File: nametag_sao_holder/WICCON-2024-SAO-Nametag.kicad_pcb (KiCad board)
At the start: 2 copper layers, 150 x 137.2 mm, 20 parts, among them J1 Conn_02x03_Odd_Even, J2 Conn_02x03_Odd_Even, J3 Conn_02x03_Odd_Even, J4 Conn_02x03_Odd_Even, J5 Conn_02x03_Odd_Even, J6 Conn_02x03_Odd_Even, J7 Conn_02x03_Odd_Even, J8 Conn_02x03_Odd_Even, SW1 ON/OFF, U1 QX2303L33E

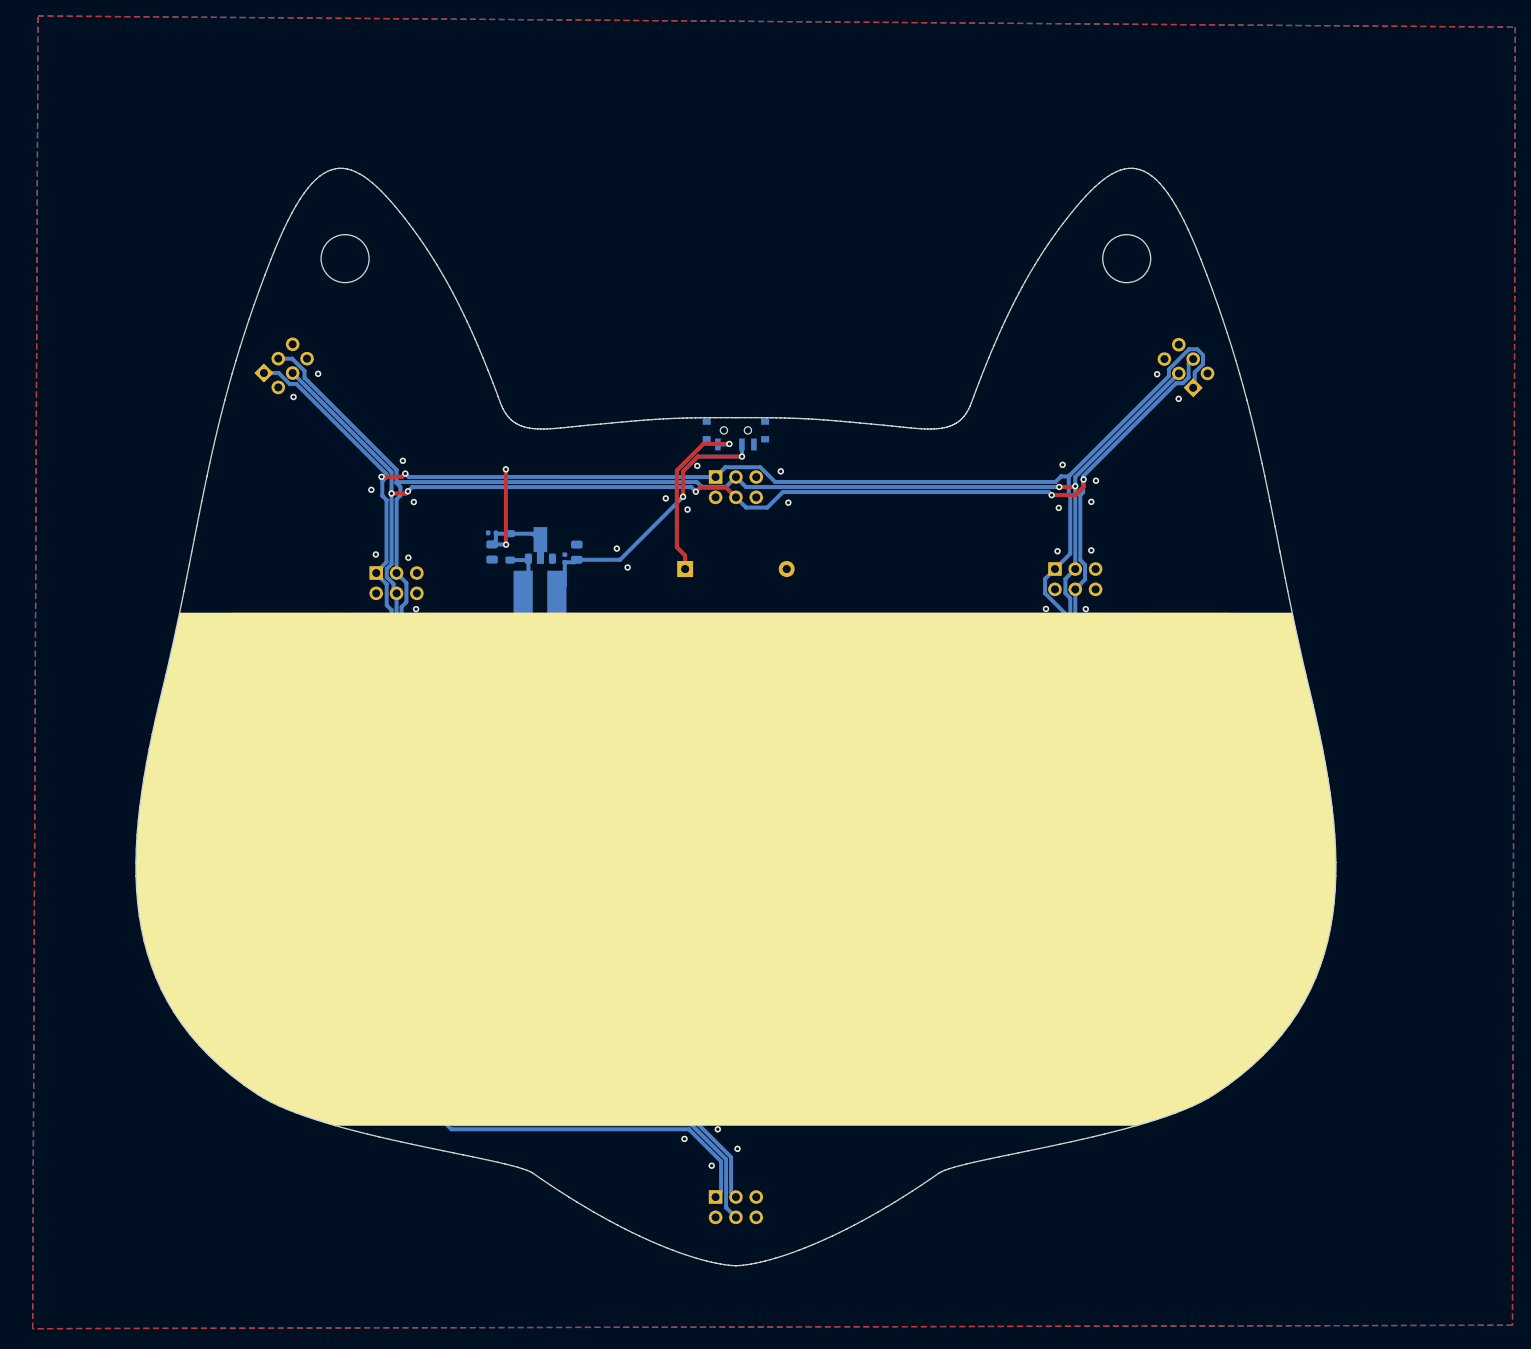
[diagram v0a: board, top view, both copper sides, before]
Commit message: Apply some improvements based on review by Paul
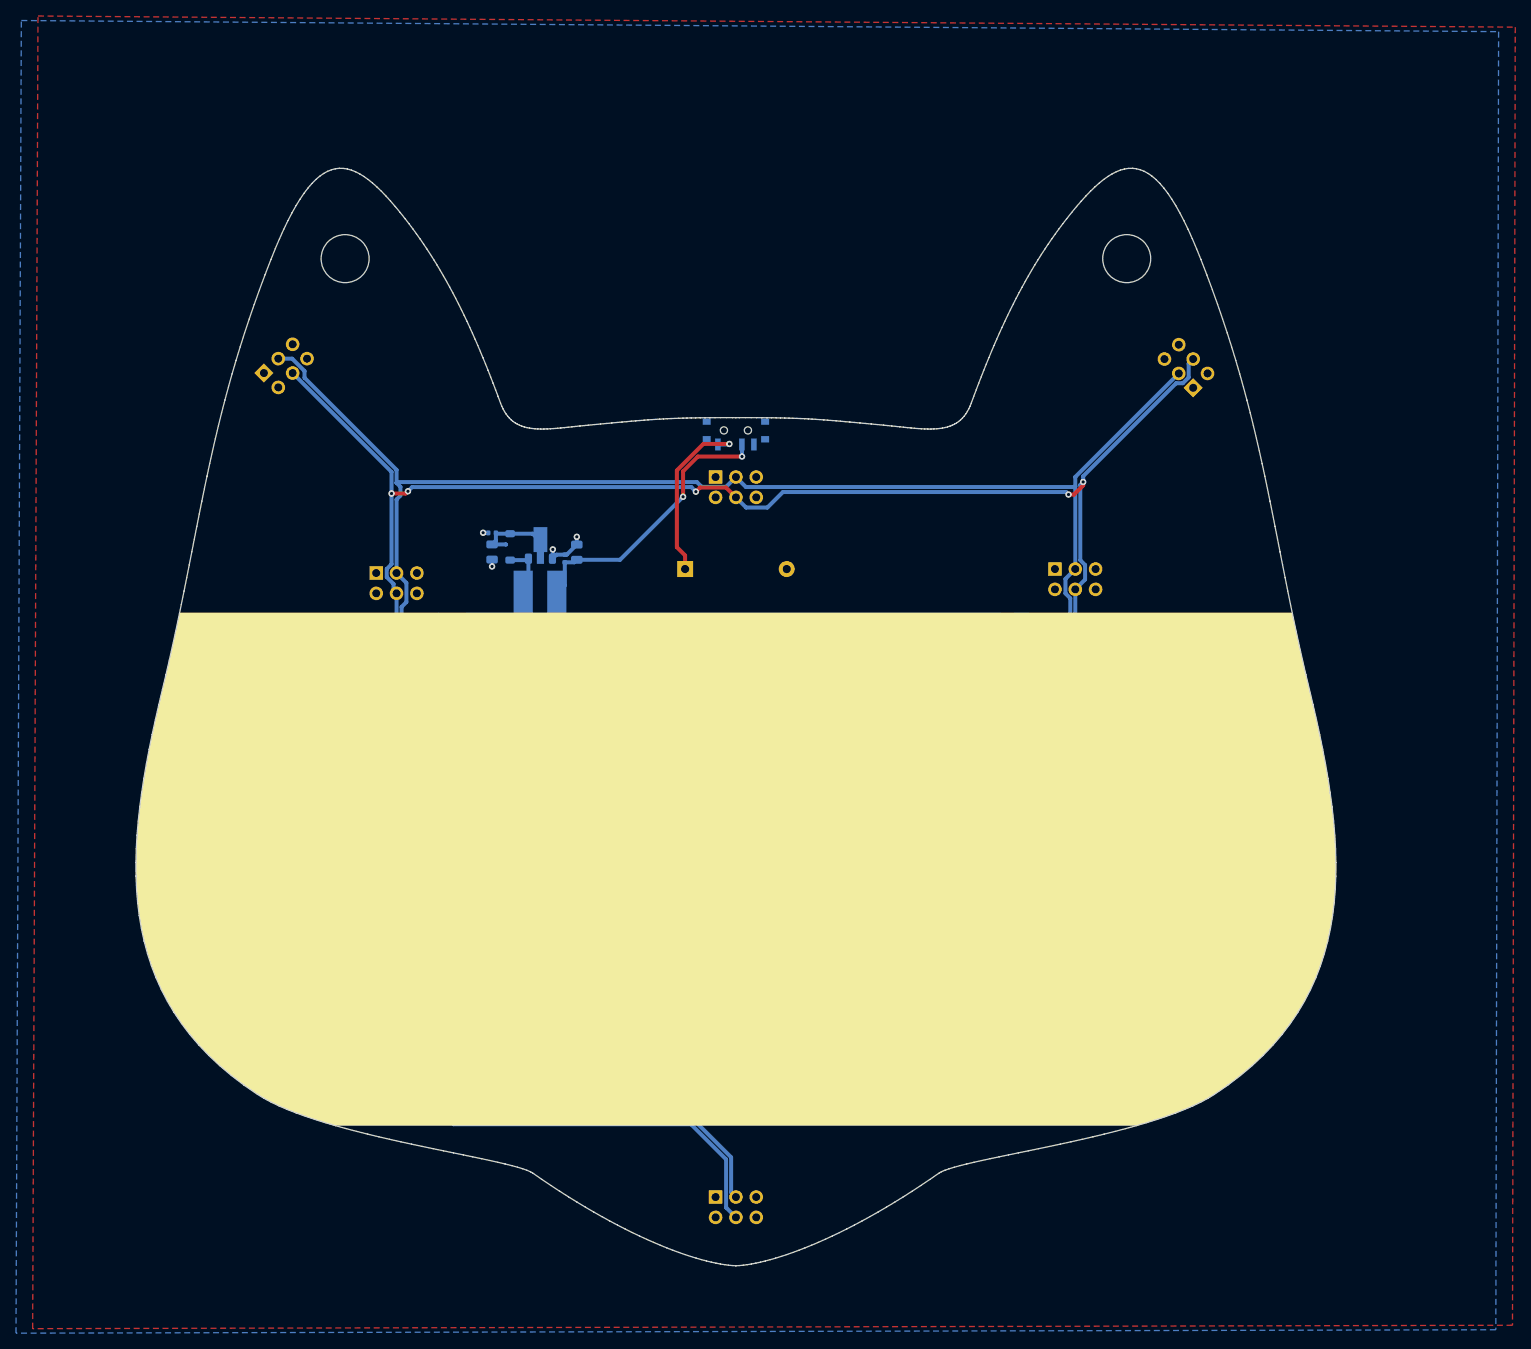
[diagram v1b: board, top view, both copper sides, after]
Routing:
- net +3.3V: track 385.5 -> 9.41 mm, vias 4 -> 0
- net GND: track 0.00 -> 7.37 mm, vias 35 -> 4
- net Net-(D1-A): track 6.97 -> 5.80 mm
- net SCL: track 348.2 -> 347.1 mm
- net SDA: vias 3 -> 1
- added copper zone on B.Cu, net +3.3V
- removed copper zone on B.Cu, net GND

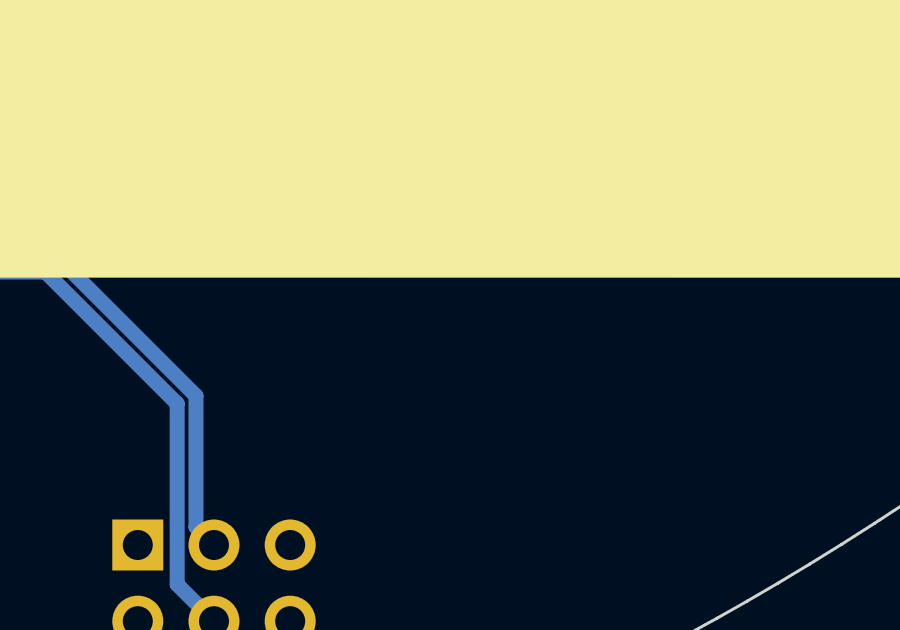
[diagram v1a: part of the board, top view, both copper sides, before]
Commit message: Added text and art
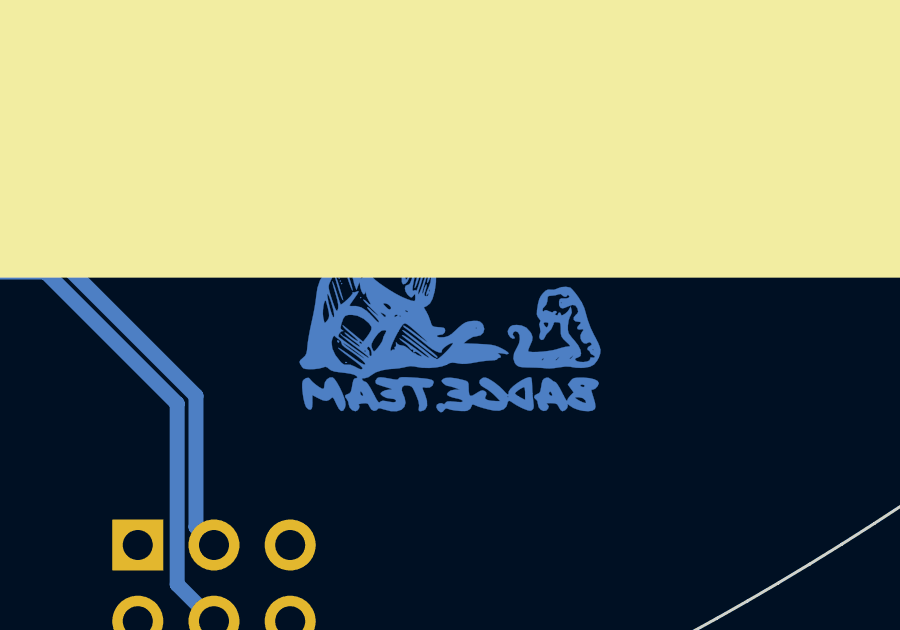
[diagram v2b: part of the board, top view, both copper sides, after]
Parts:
- added N2: badgeteam, Library:stamp, B.Cu at (7.87, 52.3)
- added N3: Sjaan, Library:Chantal, B.Cu at (0.00, -11.4)
- added N4: wicca, Library:full_wicca_logo, B.Cu at (-76.7, 46.0)
- J1, J2, J3, J4, J5, J6, J7, J8: value Conn_02x03_Odd_Even -> SAO
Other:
- board text added: "You might not be able to change the world, but you can change a small part of it."

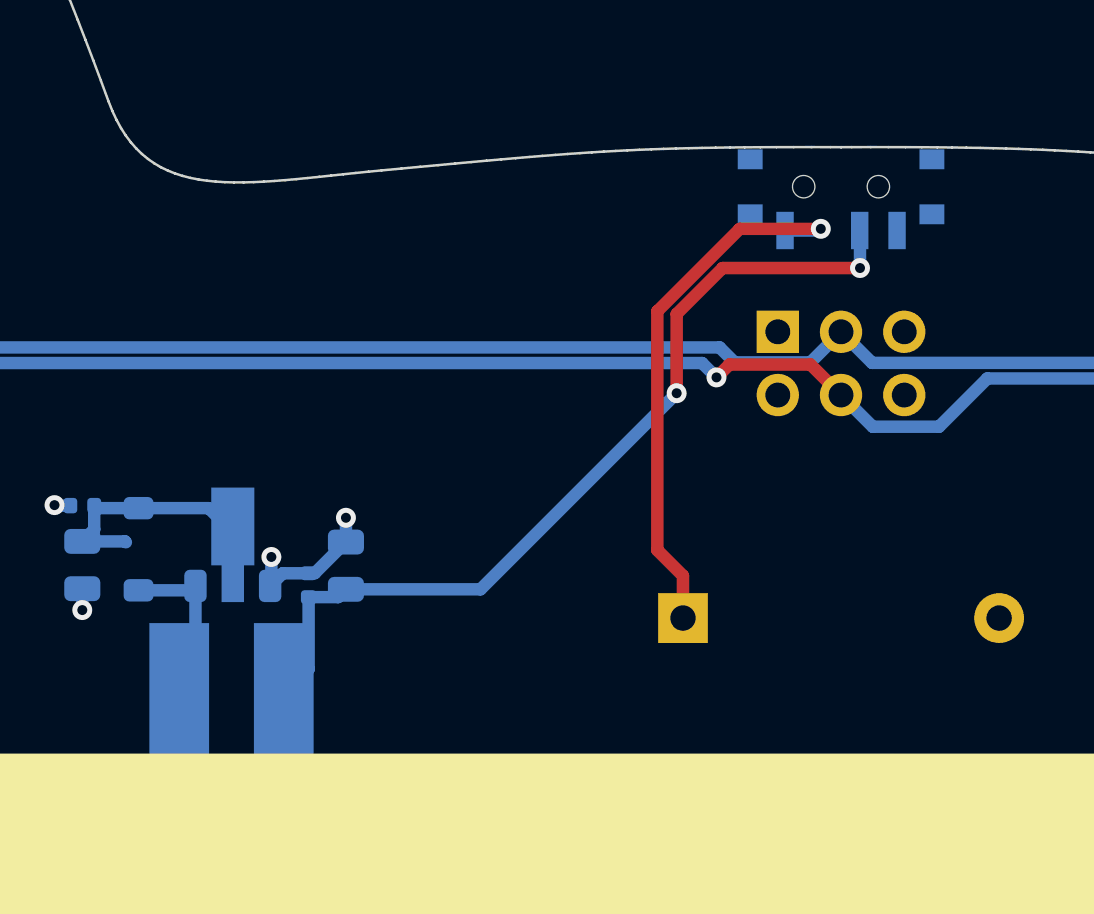
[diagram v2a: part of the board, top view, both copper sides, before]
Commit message: Small fixes, change inductor, add power LED
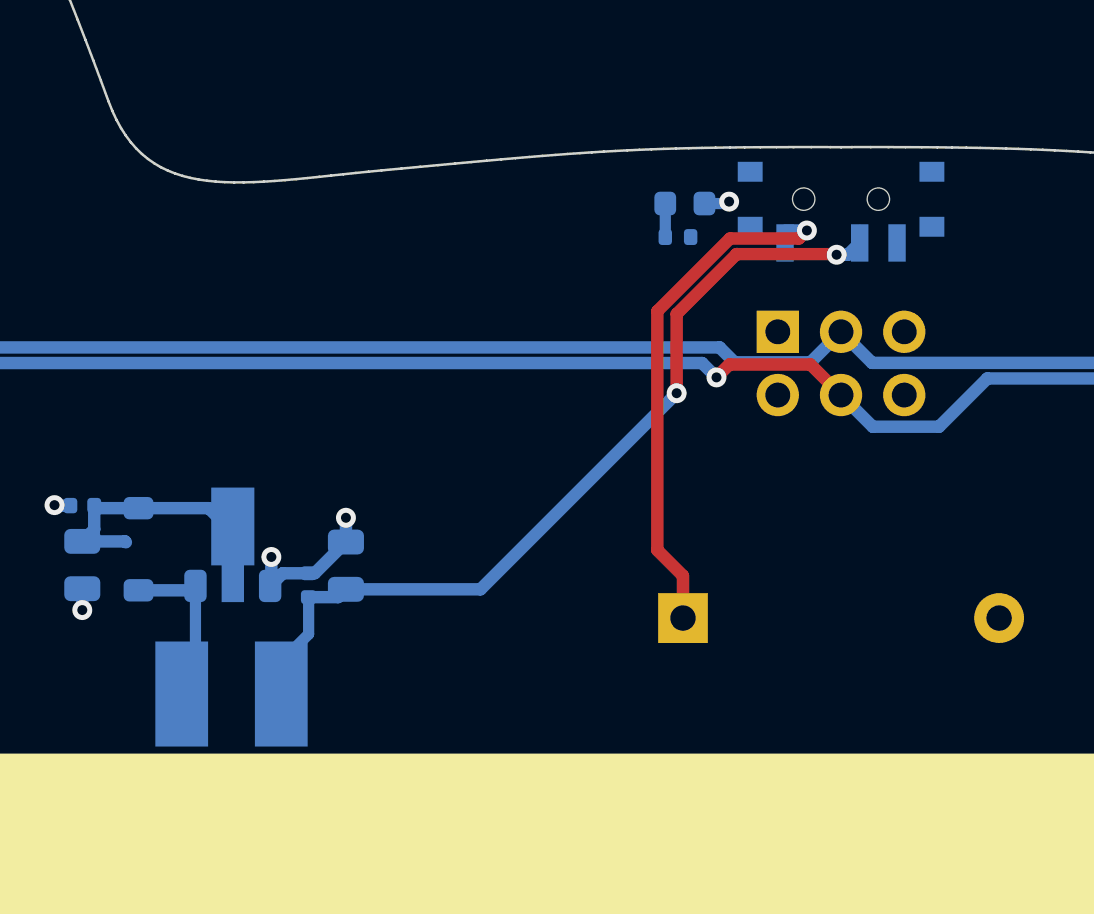
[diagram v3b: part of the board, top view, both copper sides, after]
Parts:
- added D2: RED LED, LED_SMD:LED_0603_1608Metric, B.Cu at (-6.27, -35.2)
- added R1: 330, Resistor_SMD:R_0402_1005Metric, B.Cu at (-6.55, -33.8)
- L1: footprint Inductor_SMD:L_Cenker_CKCS6020 -> Library:IND-SMD_L5.0-W5.0
- moved SW1 0.50 mm to (0.00, -35.0)
- moved N4 0.28 mm to (-77.0, 46.0)
- moved N3 0.07 mm to (0.00, -11.5)
- turned L1 to 0 degrees
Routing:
- net Net-(D1-A): track 5.80 -> 7.50 mm
- net Net-(D2-A): track 0.00 -> 1.35 mm
- net Net-(BT1-+): track 22.2 -> 21.0 mm
- net GND: track 7.37 -> 8.39 mm, vias 4 -> 5
- net Net-(SW1-B): track 35.3 -> 34.8 mm
